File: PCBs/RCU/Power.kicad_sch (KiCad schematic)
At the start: 29 parts, among them U102 AZ1117-3.3, U103 AP63203WU

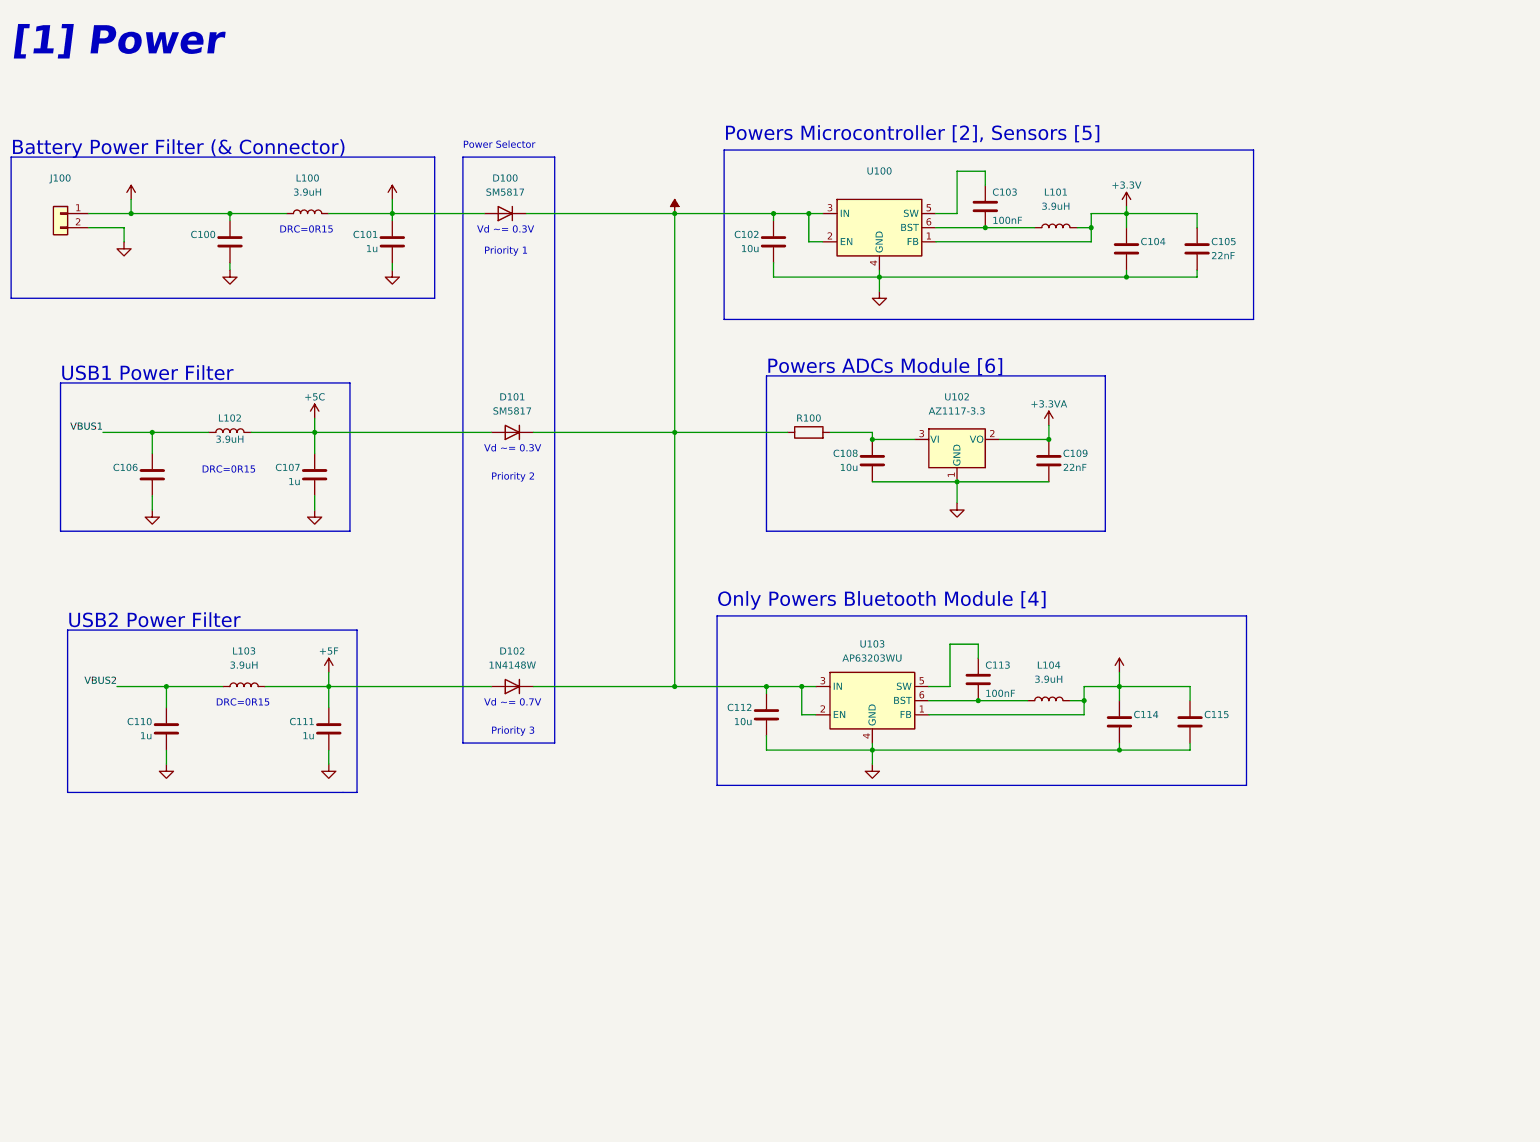
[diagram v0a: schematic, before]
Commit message: The shared SWCLK/BOOT0 pin has an internal pull-down resistor, and in the case where SWCLK is shared and are programming with SWD, just need NRST conncted to the STLink-V2 module
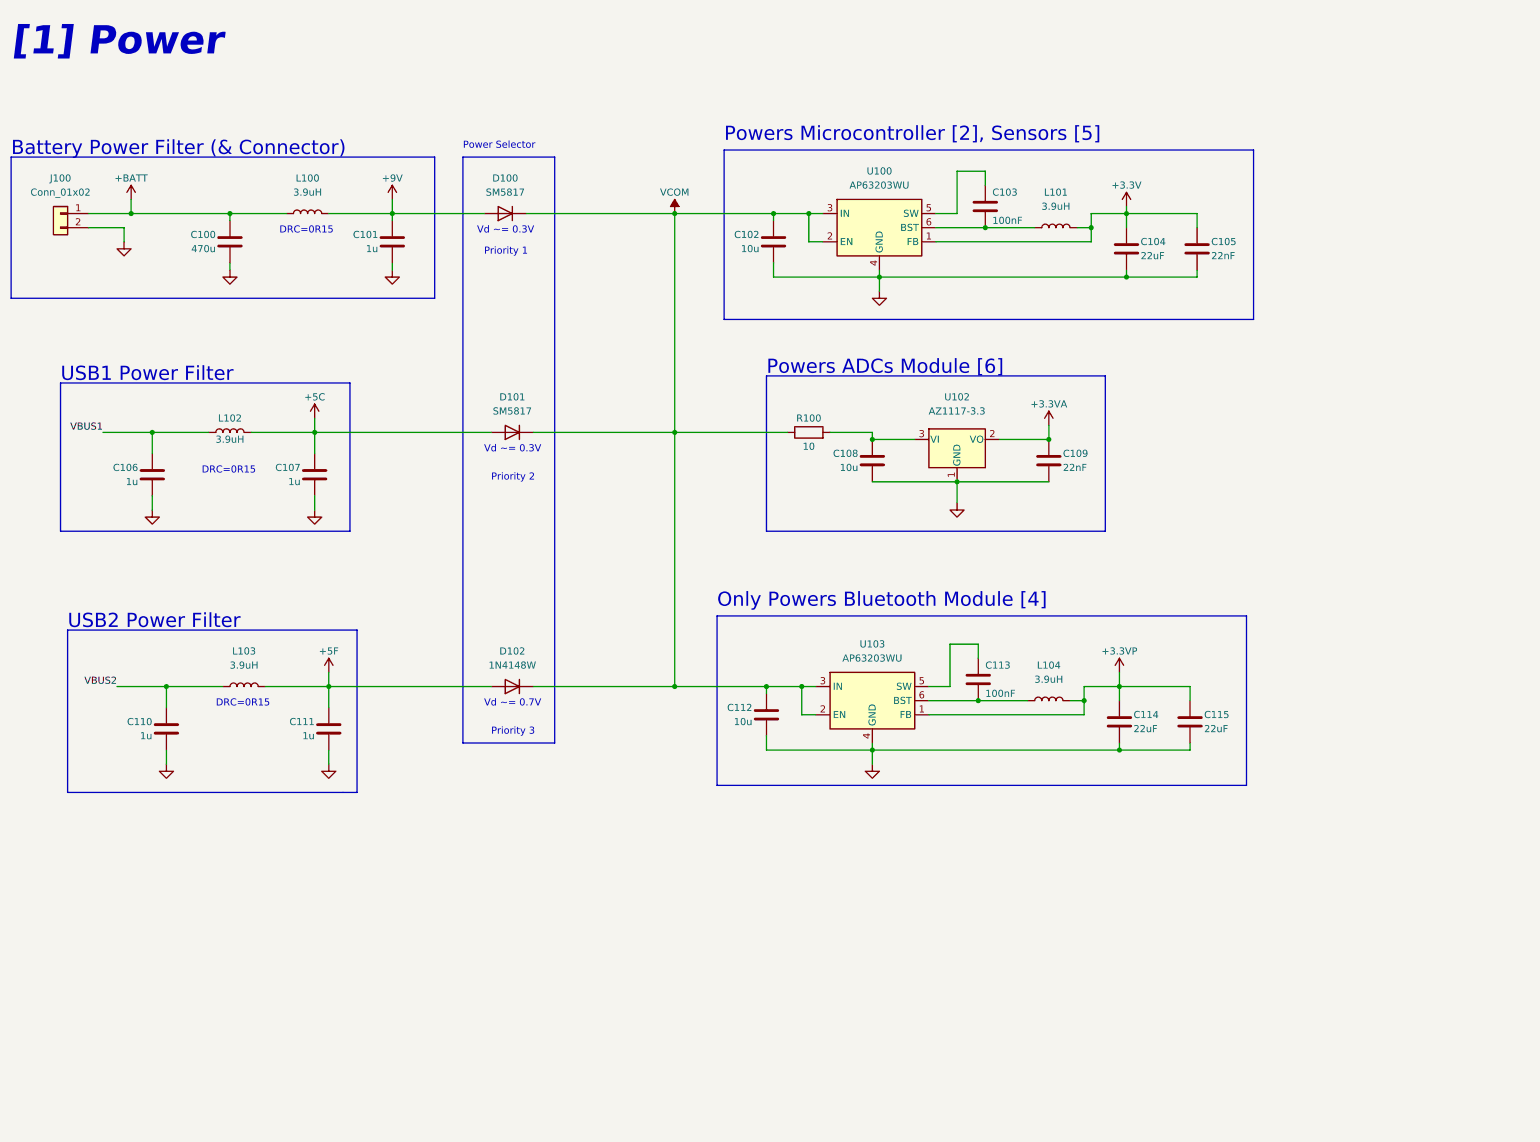
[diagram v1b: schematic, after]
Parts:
- C100: value (none) -> 470u
- C104, C114, C115: value (none) -> 22uF
- C106: value (none) -> 1u
- J100: value (none) -> Conn_01x02
- R100: value (none) -> 10
- U100: value (none) -> AP63203WU; footprint (none) -> Package_TO_SOT_SMD:TSOT-23-6
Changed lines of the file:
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@@
       (effects (font (size 1.27 1.27)) (justify left))
     )
-    (property "Value" "" (id 1) (at 227.33 148.59 0)
+    (property "Value" "22uF" (id 1) (at 227.33 148.59 0)
       (effects (font (size 1.27 1.27)) (justify left))
     )
@@
       (effects (font (size 1.27 1.27)) (justify left))
     )
-    (property "Value" "" (id 1) (at 48.26 104.14 0)
+    (property "Value" "1u" (id 1) (at 48.26 104.14 0)
       (effects (font (size 1.27 1.27)) (justify left))
     )
@@
     (in_bom yes) (on_board yes) (fields_autoplaced)
     (property "Reference" "U100" (id 0) (at 181.61 48.26 0))
-    (property "Value" "" (id 1) (at 181.61 50.8 0))
-    (property "Footprint" "" (id 2) (at 181.61 81.28 0)
+    (property "Value" "AP63203WU" (id 1) (at 181.61 50.8 0))
+    (property "Footprint" "Package_TO_SOT_SMD:TSOT-23-6" (id 2) (at 181.61 81.28 0)
       (effects (font (size 1.27 1.27)) hide)
     )
@@
       (effects (font (size 1.27 1.27)) hide)
     )
-    (property "Value" "" (id 1) (at 46.99 49.53 0))
+    (property "Value" "+BATT" (id 1) (at 46.99 49.53 0))
     (property "Footprint" "" (id 2) (at 46.99 53.34 0)
       (effects (font (size 1.27 1.27)) hide)
@@
       (effects (font (size 1.27 1.27)) hide)
     )
-    (property "Value" "" (id 1) (at 144.78 52.07 0))
+    (property "Value" "VCOM" (id 1) (at 144.78 52.07 0))
     (property "Footprint" "" (id 2) (at 144.78 55.88 0)
       (effects (font (size 1.27 1.27)) hide)
@@
       (effects (font (size 1.27 1.27)) hide)
     )
-    (property "Value" "" (id 1) (at 93.98 49.53 0))
+    (property "Value" "+9V" (id 1) (at 93.98 49.53 0))
     (property "Footprint" "" (id 2) (at 93.98 53.34 0)
       (effects (font (size 1.27 1.27)) hide)
@@
     (in_bom yes) (on_board yes) (fields_autoplaced)
     (property "Reference" "J100" (id 0) (at 34.29 49.53 0))
-    (property "Value" "" (id 1) (at 34.29 52.07 0))
+    (property "Value" "Conn_01x02" (id 1) (at 34.29 52.07 0))
     (property "Footprint" "" (id 2) (at 34.29 55.88 0)
       (effects (font (size 1.27 1.27)) hide)
@@
     (in_bom yes) (on_board yes)
     (property "Reference" "R100" (id 0) (at 168.91 92.71 90))
-    (property "Value" "" (id 1) (at 168.91 97.79 90))
+    (property "Value" "10" (id 1) (at 168.91 97.79 90))
     (property "Footprint" "" (id 2) (at 168.91 97.028 90)
       (effects (font (size 1.27 1.27)) hide)
@@
       (effects (font (size 1.27 1.27)) (justify left))
     )
-    (property "Value" "" (id 1) (at 228.6 63.5 0)
+    (property "Value" "22uF" (id 1) (at 228.6 63.5 0)
       (effects (font (size 1.27 1.27)) (justify left))
     )
@@
       (effects (font (size 1.27 1.27)) (justify left))
     )
-    (property "Value" "" (id 1) (at 62.23 62.23 0)
+    (property "Value" "470u" (id 1) (at 62.23 62.23 0)
       (effects (font (size 1.27 1.27)) (justify left))
     )
@@
       (effects (font (size 1.27 1.27)) (justify left))
     )
-    (property "Value" "" (id 1) (at 240.03 148.59 0)
+    (property "Value" "22uF" (id 1) (at 240.03 148.59 0)
       (effects (font (size 1.27 1.27)) (justify left))
     )
@@
       (effects (font (size 1.27 1.27)) hide)
     )
-    (property "Value" "" (id 1) (at 224.79 134.62 0))
+    (property "Value" "+3.3VP" (id 1) (at 224.79 134.62 0))
     (property "Footprint" "" (id 2) (at 224.79 138.43 0)
       (effects (font (size 1.27 1.27)) hide)

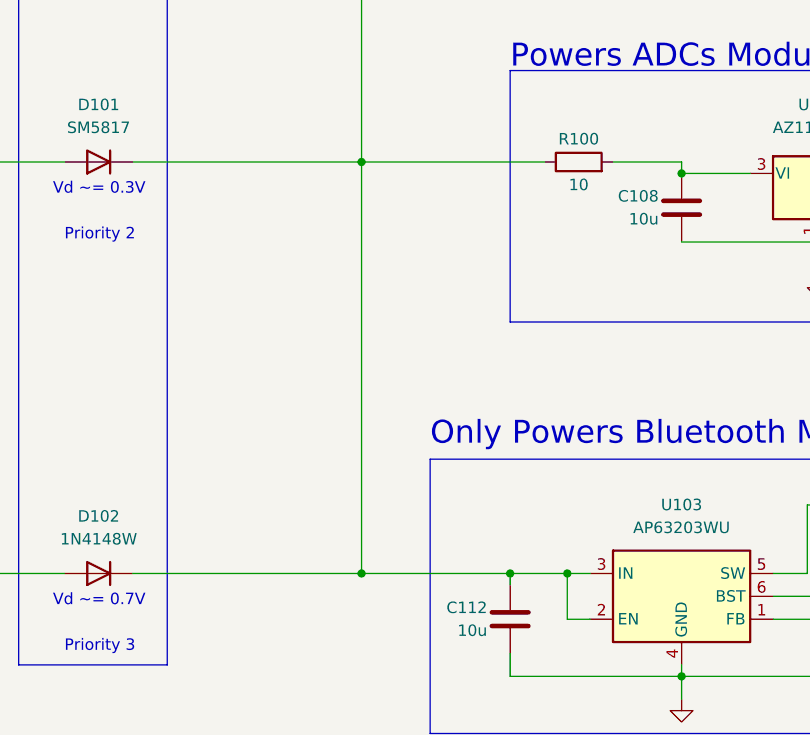
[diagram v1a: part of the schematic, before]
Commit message: Add Diode to ensure USB2 only power Bluetooth module
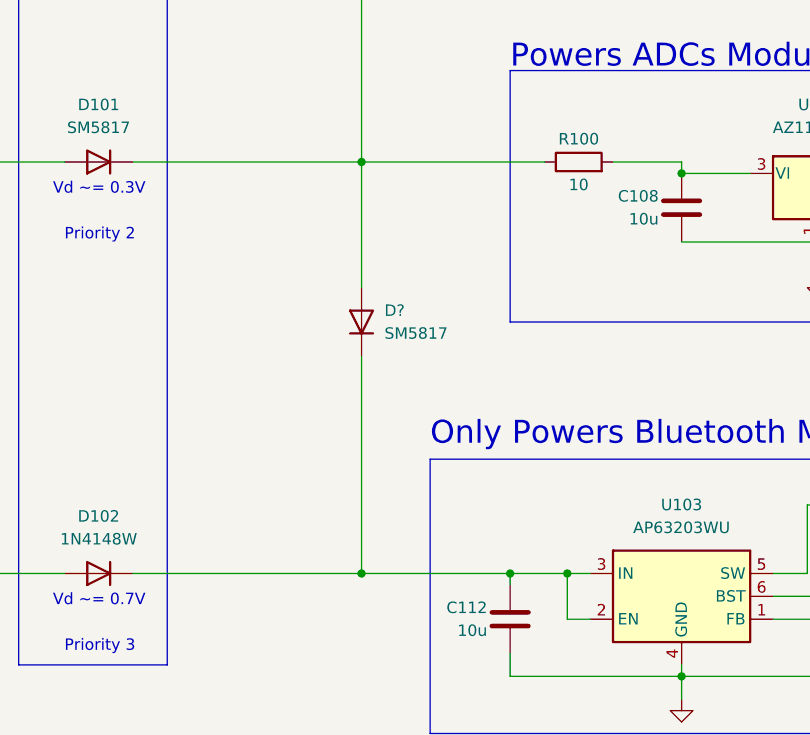
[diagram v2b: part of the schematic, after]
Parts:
- added D?: SM5817, symbol Diode:SM513
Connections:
- net VCOM: now also D?.2 (A); no longer C112.1, D102.1 (K), U103.2 (EN), U103.3 (IN)
- new net: C112.1, D102.1 (K), D?.1 (K), U103.2 (EN), U103.3 (IN)
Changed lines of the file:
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@@
   (junction (at 181.61 67.31) (diameter 0) (color 0 0 0 0)
   )
+  (junction (at 224.79 140.97) (diameter 0) (color 0 0 0 0)
+  )
+  (junction (at 226.06 67.31) (diameter 0) (color 0 0 0 0)
+  )
+  (junction (at 212.09 96.52) (diameter 0) (color 0 0 0 0)
+  )
+  (junction (at 82.55 140.97) (diameter 0) (color 0 0 0 0)
+  )
+  (junction (at 80.01 95.25) (diameter 0) (color 0 0 0 0)
+  )
+  (junction (at 161.29 140.97) (diameter 0) (color 0 0 0 0)
+  )
+  (junction (at 144.78 95.25) (diameter 0) (color 0 0 0 0)
+  )
+  (junction (at 50.8 95.25) (diameter 0) (color 0 0 0 0)
+  )
+  (junction (at 162.56 55.88) (diameter 0) (color 0 0 0 0)
+  )
+  (junction (at 93.98 55.88) (diameter 0) (color 0 0 0 0)
+  )
   (junction (at 144.78 140.97) (diameter 0) (color 0 0 0 0)
   )
-  (junction (at 224.79 140.97) (diameter 0) (color 0 0 0 0)
-  )
-  (junction (at 226.06 67.31) (diameter 0) (color 0 0 0 0)
-  )
-  (junction (at 212.09 96.52) (diameter 0) (color 0 0 0 0)
-  )
-  (junction (at 82.55 140.97) (diameter 0) (color 0 0 0 0)
-  )
-  (junction (at 80.01 95.25) (diameter 0) (color 0 0 0 0)
-  )
-  (junction (at 161.29 140.97) (diameter 0) (color 0 0 0 0)
-  )
-  (junction (at 144.78 95.25) (diameter 0) (color 0 0 0 0)
-  )
-  (junction (at 50.8 95.25) (diameter 0) (color 0 0 0 0)
-  )
-  (junction (at 162.56 55.88) (diameter 0) (color 0 0 0 0)
-  )
-  (junction (at 93.98 55.88) (diameter 0) (color 0 0 0 0)
-  )
   (junction (at 226.06 55.88) (diameter 0) (color 0 0 0 0)
   )
@@
     (stroke (width 0) (type default) (color 0 0 0 0))
   )
+  (wire (pts (xy 144.78 140.97) (xy 161.29 140.97))
+    (stroke (width 0) (type default) (color 0 0 0 0))
+  )
   (wire (pts (xy 226.06 55.88) (xy 226.06 58.42))
     (stroke (width 0) (type default) (color 0 0 0 0))
@@
     (stroke (width 0) (type default) (color 0 0 0 0))
   )
+  (wire (pts (xy 144.78 116.84) (xy 144.78 140.97))
+    (stroke (width 0) (type default) (color 0 0 0 0))
+  )
   (wire (pts (xy 168.91 55.88) (xy 162.56 55.88))
     (stroke (width 0) (type default) (color 0 0 0 0))
@@
     (stroke (width 0) (type default) (color 0 0 0 0))
   )
-  (wire (pts (xy 144.78 95.25) (xy 144.78 140.97))
-    (stroke (width 0) (type default) (color 0 0 0 0))
-  )
   (wire (pts (xy 53.34 140.97) (xy 53.34 144.78))
     (stroke (width 0) (type default) (color 0 0 0 0))
@@
     (stroke (width 0) (type default) (color 0 0 0 0))
   )
-  (wire (pts (xy 144.78 140.97) (xy 161.29 140.97))
-    (stroke (width 0) (type default) (color 0 0 0 0))
-  )
   (wire (pts (xy 93.98 66.04) (xy 93.98 64.77))
     (stroke (width 0) (type default) (color 0 0 0 0))
@@
   )
   (wire (pts (xy 238.76 58.42) (xy 238.76 55.88))
+    (stroke (width 0) (type default) (color 0 0 0 0))
+  )
+  (wire (pts (xy 144.78 95.25) (xy 144.78 109.22))
     (stroke (width 0) (type default) (color 0 0 0 0))
   )
@@
     (pin "1")
   )
+  (symbol (lib_id "Diode:SM513") (at 144.78 113.03 90) (unit 1)
+    (in_bom yes) (on_board yes) (fields_autoplaced)
+    (property "Reference" "D?" (id 0) (at 147.32 111.7599 90)
+      (effects (font (size 1.27 1.27)) (justify right))
+    )
+    (property "Value" "SM5817" (id 1) (at 147.32 114.2999 90)
+      (effects (font (size 1.27 1.27)) (justify right))
+    )
+    (property "Footprint" "" (id 2) (at 149.225 113.03 0)
+      (effects (font (size 1.27 1.27)) hide)
+    )
+    (property "Datasheet" "http://cdn-reichelt.de/documents/datenblatt/A400/SMD1N400%23DIO.pdf" (id 3) (at 144.78 113.03 0)
+      (effects (font (size 1.27 1.27)) hide)
+    )
+    (pin "1")
+    (pin "2")
+  )
   (symbol (lib_id "Device:C") (at 237.49 147.32 0) (unit 1)

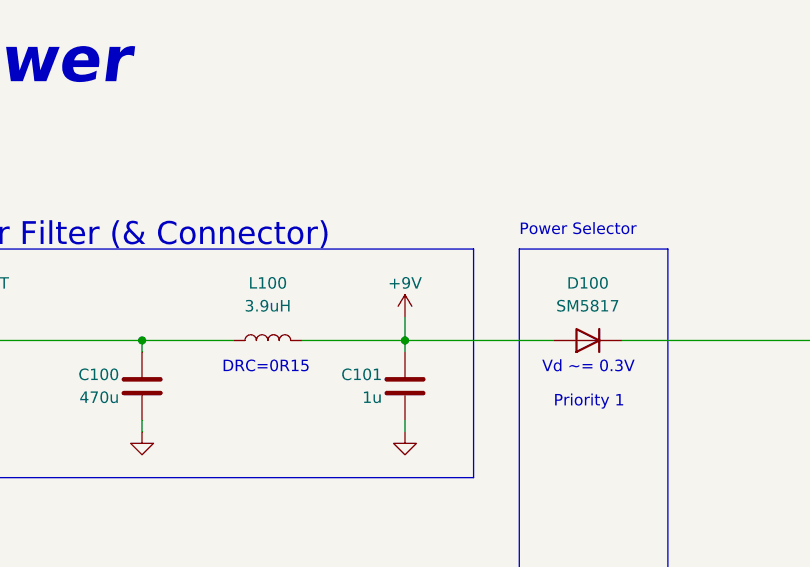
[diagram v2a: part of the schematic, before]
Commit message: Will use a 6V battery instead of 9V, since motor I am using is rated for 6V
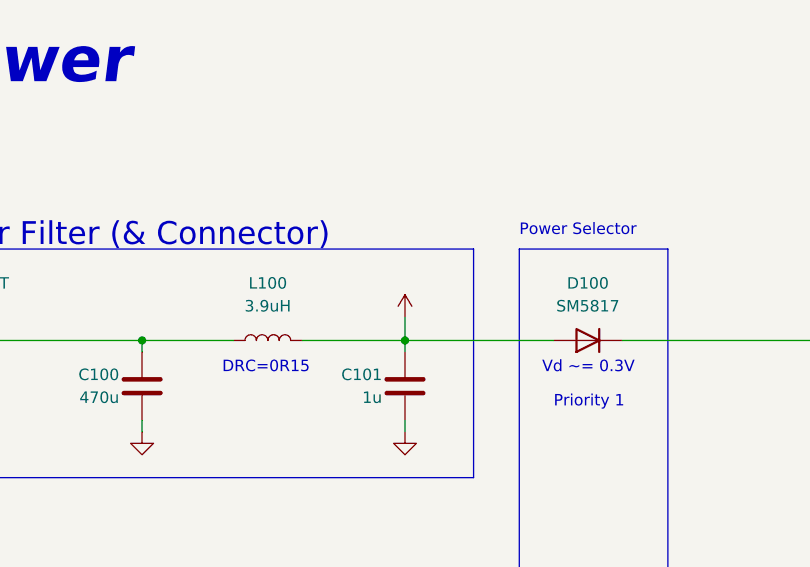
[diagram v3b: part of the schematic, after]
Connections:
- net +9V renamed +6V
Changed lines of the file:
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@@
-    (pin "1")
-  )
-  (symbol (lib_id "power:+9V") (at 93.98 53.34 0) (unit 1)
-    (in_bom yes) (on_board yes)
-    (property "Reference" "#PWR?" (id 0) (at 93.98 57.15 0)
-      (effects (font (size 1.27 1.27)) hide)
-    )
-    (property "Value" "+9V" (id 1) (at 93.98 49.53 0))
-    (property "Footprint" "" (id 2) (at 93.98 53.34 0)
-      (effects (font (size 1.27 1.27)) hide)
-    )
-    (property "Datasheet" "" (id 3) (at 93.98 53.34 0)
-      (effects (font (size 1.27 1.27)) hide)
-    )
     (pin "1")
   )
@@
     (pin "2")
   )
+  (symbol (lib_id "power:+6V") (at 93.98 53.34 0) (unit 1)
+    (in_bom yes) (on_board yes)
+    (property "Reference" "#PWR?" (id 0) (at 93.98 57.15 0)
+      (effects (font (size 1.27 1.27)) hide)
+    )
+    (property "Value" "" (id 1) (at 93.98 49.53 0))
+    (property "Footprint" "" (id 2) (at 93.98 53.34 0)
+      (effects (font (size 1.27 1.27)) hide)
+    )
+    (property "Datasheet" "" (id 3) (at 93.98 53.34 0)
+      (effects (font (size 1.27 1.27)) hide)
+    )
+    (pin "1")
+  )
   (symbol (lib_id "Device:C") (at 64.77 60.96 0) (mirror y) (unit 1)
